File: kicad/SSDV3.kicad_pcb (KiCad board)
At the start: 4 copper layers, 58.4 x 28.8 mm, 69 parts, among them J1 SolderPad, J2 SolderPad, J3 SolderPad, J4 SolderPad, J5 SolderPad, J6 SolderPad, J7 SM02B-GHS-TB(LF)(SN), J8 SM03B-GHS-TB(LF)(SN), Q1 BSZ146N10LS5, Q2 BSZ146N10LS5, Q3 BSZ146N10LS5, U1 LM5050-1, U2 LM5146

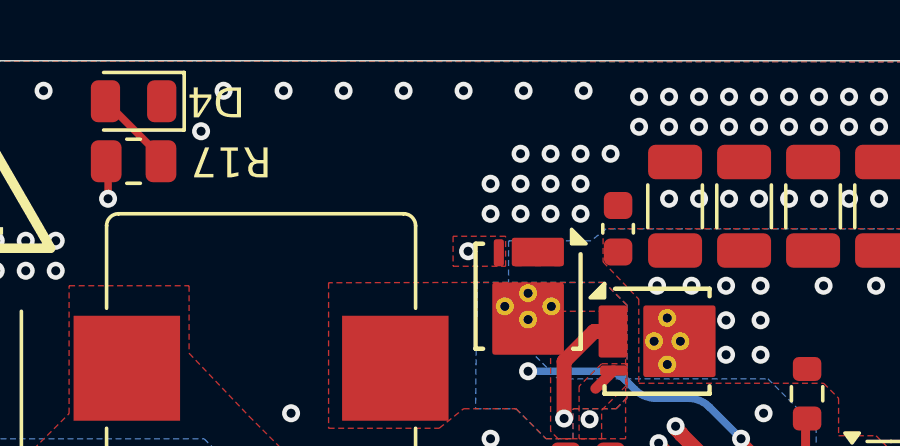
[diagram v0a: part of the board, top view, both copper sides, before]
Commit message: Added UBCO trademark notice, prepared for production
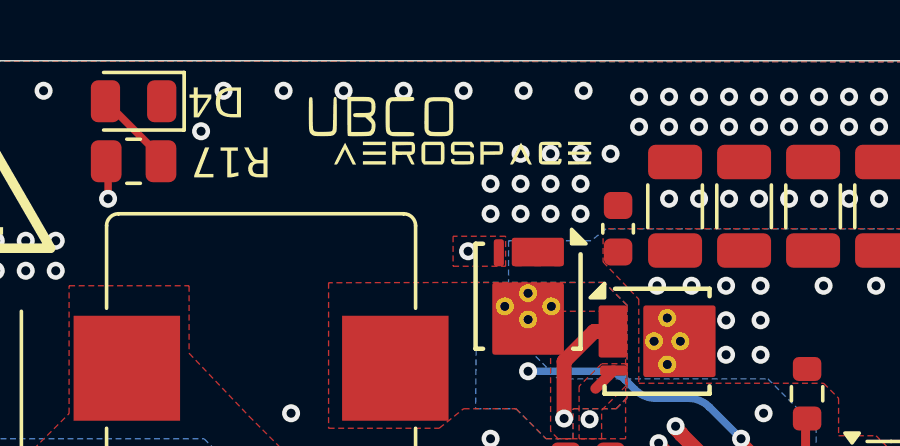
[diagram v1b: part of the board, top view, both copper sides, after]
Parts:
- added G***: LOGO, LOGO, F.Cu at (147.3, 102.3)
- added G***: LOGO, LOGO, B.Cu at (140.8, 107.2)
- added G***: LOGO, LOGO, B.Cu at (146.0, 120.8)
- moved G*** 4.53 mm to (146.0, 114.5)
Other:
- board text added: "CAUTION 50V SYSTEM"

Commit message: Component optimizations
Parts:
- C18, C19, C20, C21, C22, C23: footprint Capacitor_SMD:C_1206_3216Metric -> Capacitor_SMD:C_1206_3216Metric_Pad1.33x1.80mm_HandSolder
- R16: footprint Resistor_SMD:R_0603_1608Metric -> Resistor_SMD:R_0603_1608Metric_Pad0.98x0.95mm_HandSolder
- moved C24 1.00 mm to (130.8, 111.0)
- moved R16 0.25 mm to (153.9, 122.1)
- moved C18 0.25 mm to (139.7, 119.5)
- moved C19 0.25 mm to (137.4, 119.5)
- moved C20 0.25 mm to (135.1, 119.5)
- moved C21 0.25 mm to (142.0, 119.5)
- moved C22 0.25 mm to (130.5, 119.5)
- moved C23 0.25 mm to (132.8, 119.5)
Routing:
- net PGND: vias 134 -> 133
